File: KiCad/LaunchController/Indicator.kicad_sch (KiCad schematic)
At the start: 44 parts

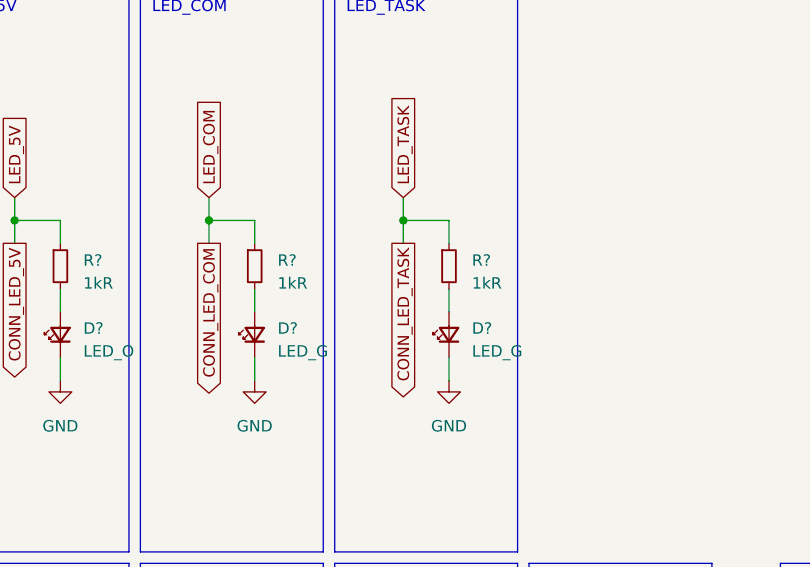
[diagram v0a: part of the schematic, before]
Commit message: イラン分圧回路を削除
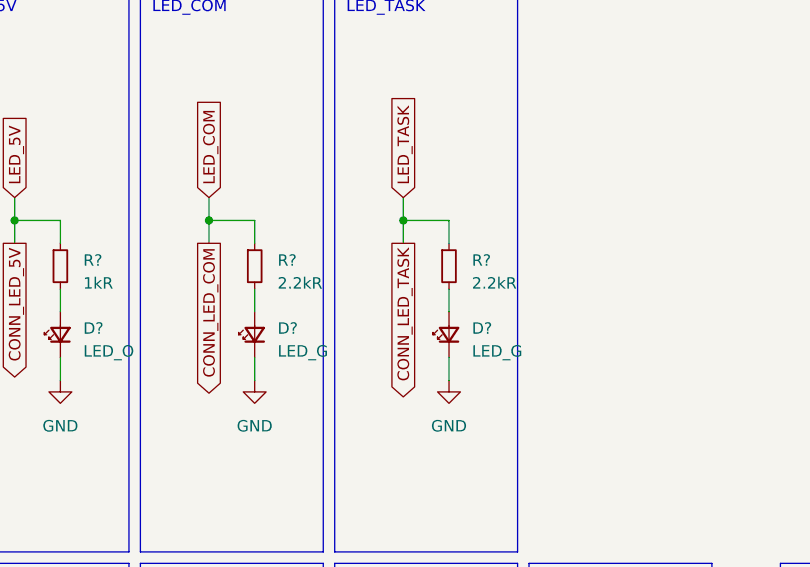
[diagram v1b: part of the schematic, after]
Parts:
- R? (x2): value 1kR -> 2.2kR
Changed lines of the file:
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@@
       (effects (font (size 1.27 1.27)) (justify left))
     )
-    (property "Value" "1kR" (at 114.3 45.085 0)
+    (property "Value" "2.2kR" (at 114.3 45.085 0)
       (effects (font (size 1.27 1.27)) (justify left))
     )
@@
       (effects (font (size 1.27 1.27)) (justify left))
     )
-    (property "Value" "1kR" (at 92.71 45.085 0)
+    (property "Value" "2.2kR" (at 92.71 45.085 0)
       (effects (font (size 1.27 1.27)) (justify left))
     )

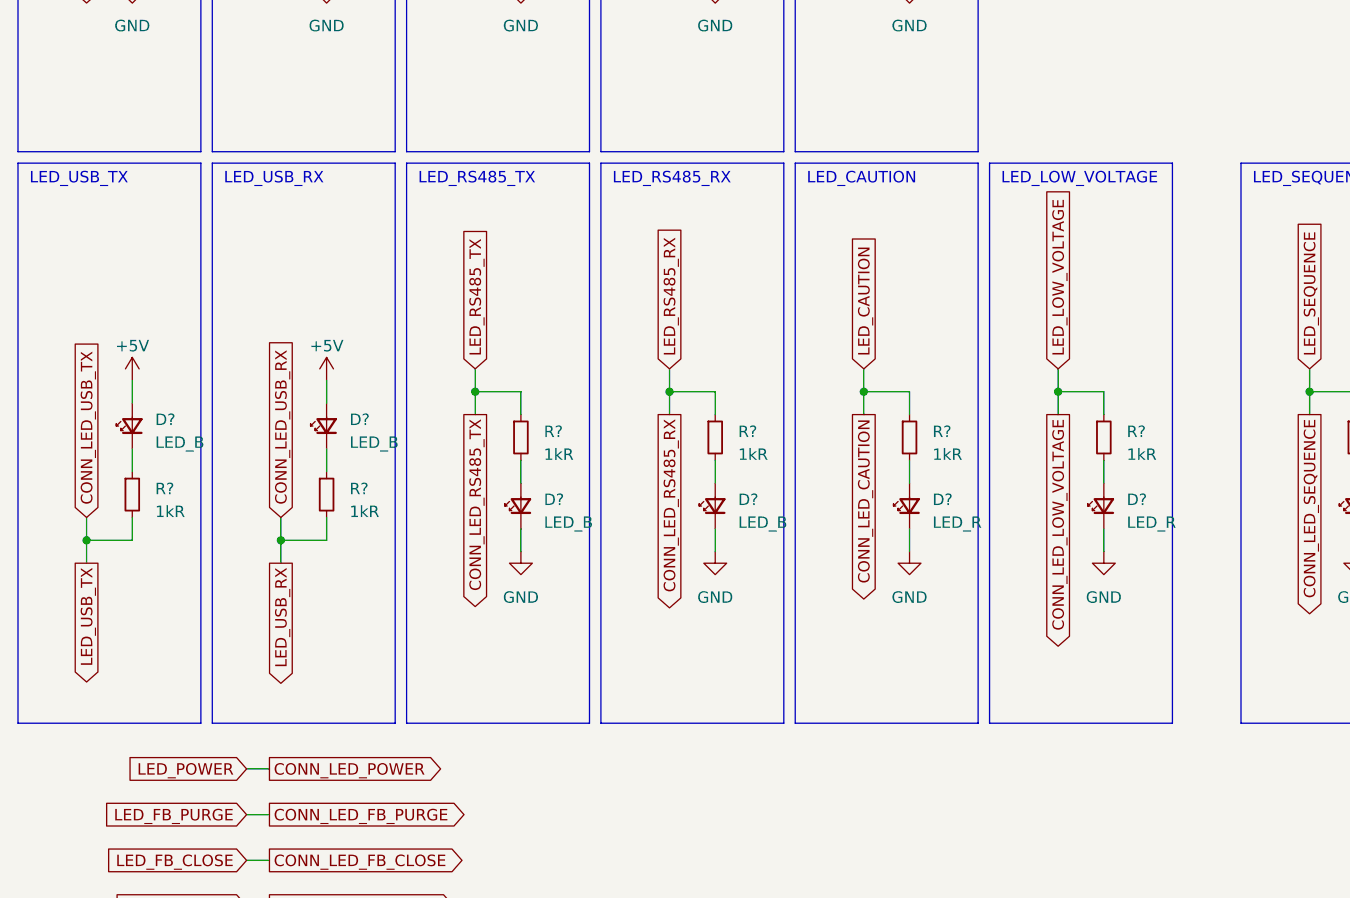
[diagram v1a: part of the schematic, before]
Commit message: USBのTX，RXを統合してACCESSに変更
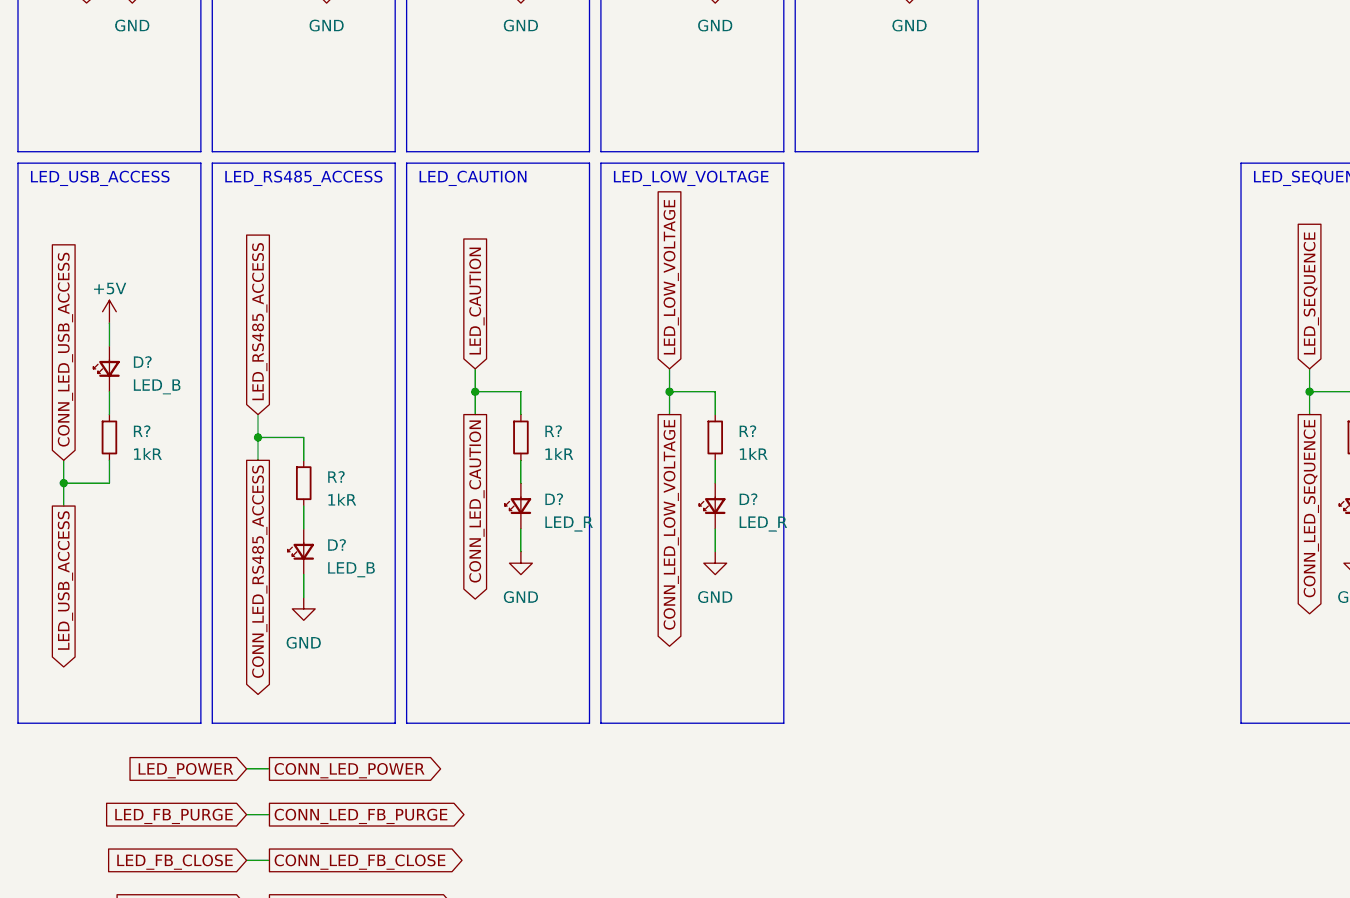
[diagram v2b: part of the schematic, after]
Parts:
- removed D? (x2): LED_B, LED_SMD:LED_0603_1608Metric_Pad1.05x0.95mm_HandSolder, symbol Device:LED_Small
- removed R? (x2): 1kR, Resistor_SMD:R_0603_1608Metric_Pad0.98x0.95mm_HandSolder, symbol Device:R_Small
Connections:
- net CONN_LED_RS485_TX renamed CONN_LED_RS485_ACCESS
- net CONN_LED_USB_TX renamed CONN_LED_USB_ACCESS
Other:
- note added: "LED_RS485_ACCESS"
- note added: "LED_USB_ACCESS"
- note removed: "LED_RS485_RX"
- note removed: "LED_RS485_TX"
- note removed: "LED_USB_RX"
- note removed: "LED_USB_TX"
- moved on the sheet: D?, R?

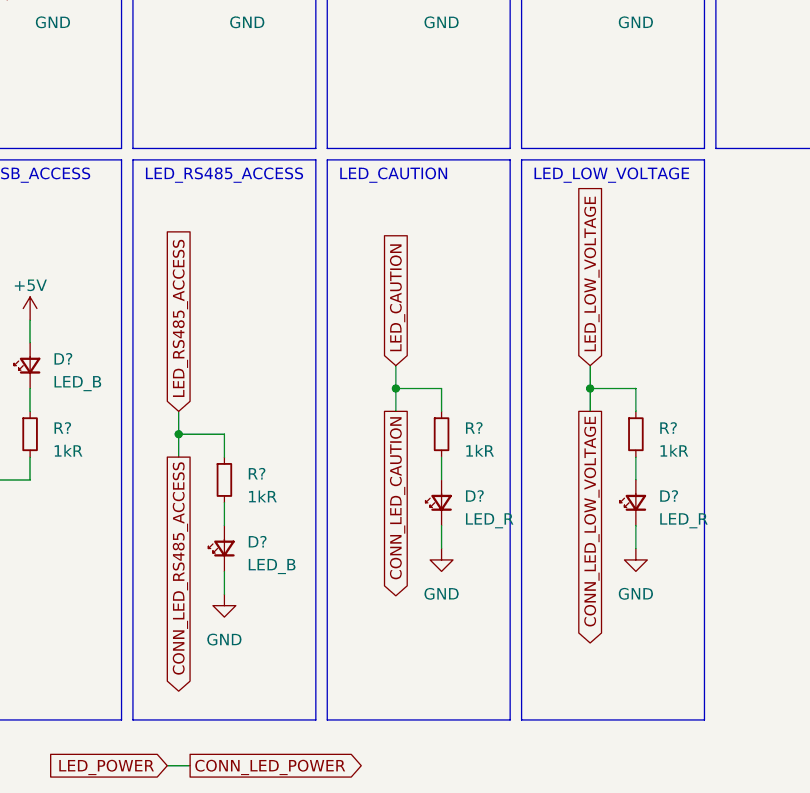
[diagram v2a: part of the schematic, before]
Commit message: CAUTIONをERRORに名称変更
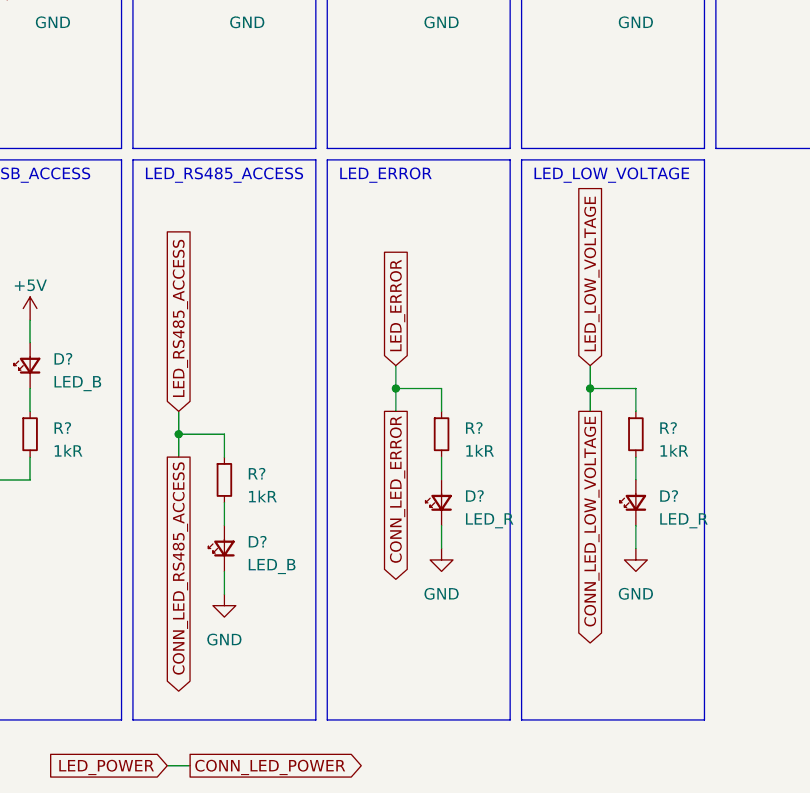
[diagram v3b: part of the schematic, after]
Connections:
- net CONN_LED_CAUTION renamed CONN_LED_ERROR
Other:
- note added: "LED_ERROR"
- note removed: "LED_CAUTION"
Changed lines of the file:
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@@
     (effects (font (size 1.27 1.27)) (justify left bottom))
   )
-  (text "LED_CAUTION" (at 57.15 78.74 0)
+  (text "LED_ERROR" (at 57.15 78.74 0)
     (effects (font (size 1.27 1.27)) (justify left bottom))
   )
@@
     )
   )
-  (global_label "CONN_LED_CAUTION" (shape output) (at 63.5 104.14 270) (fields_autoplaced)
-    (effects (font (size 1.27 1.27)) (justify right))
-    (property "Intersheetrefs" "${INTERSHEET_REFS}" (at 63.5 125.6121 90)
+  (global_label "CONN_LED_ERROR" (shape output) (at 63.5 104.14 270) (fields_autoplaced)
+    (effects (font (size 1.27 1.27)) (justify right))
+    (property "Intersheetrefs" "${INTERSHEET_REFS}" (at 63.5 123.9791 90)
       (effects (font (size 1.27 1.27)) (justify right) hide)
     )
@@
     )
   )
-  (global_label "LED_CAUTION" (shape input) (at 63.5 99.06 90) (fields_autoplaced)
-    (effects (font (size 1.27 1.27)) (justify left))
-    (property "Intersheetrefs" "${INTERSHEET_REFS}" (at 63.5 83.817 90)
-      (effects (font (size 1.27 1.27)) (justify left) hide)
-    )
+  (global_label "LED_ERROR" (shape input) (at 63.5 99.06 90) (fields_autoplaced)
+    (effects (font (size 1.27 1.27)) (justify left))
+    (property "Intersheetrefs" "${INTERSHEET_REFS}" (at 63.5 85.45 90)
+      (effects (font (size 1.27 1.27)) (justify left) hide)
+    )

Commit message: KiCad9.0に対応
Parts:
- gave numbers to parts that had none: 40
